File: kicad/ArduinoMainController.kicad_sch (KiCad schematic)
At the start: 3 parts

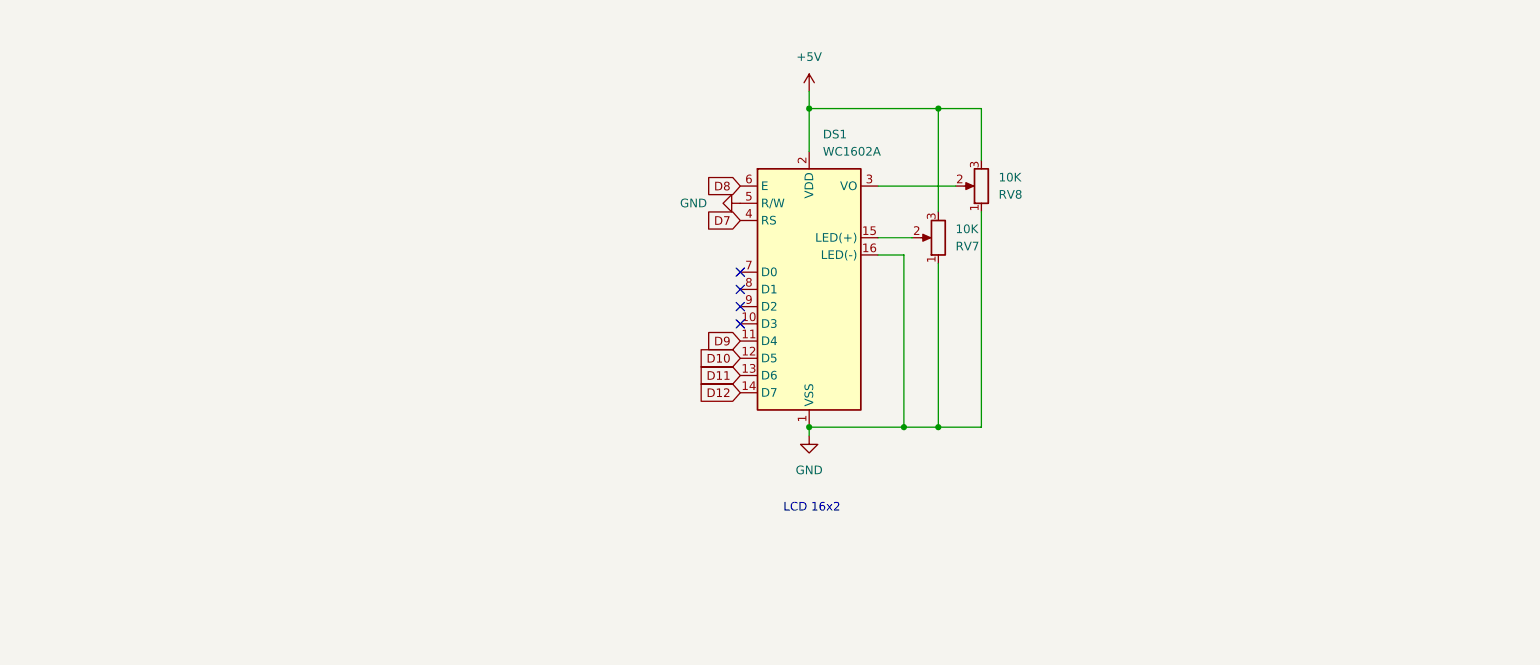
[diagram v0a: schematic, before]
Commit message: Cambio Arduino por el ATMega328
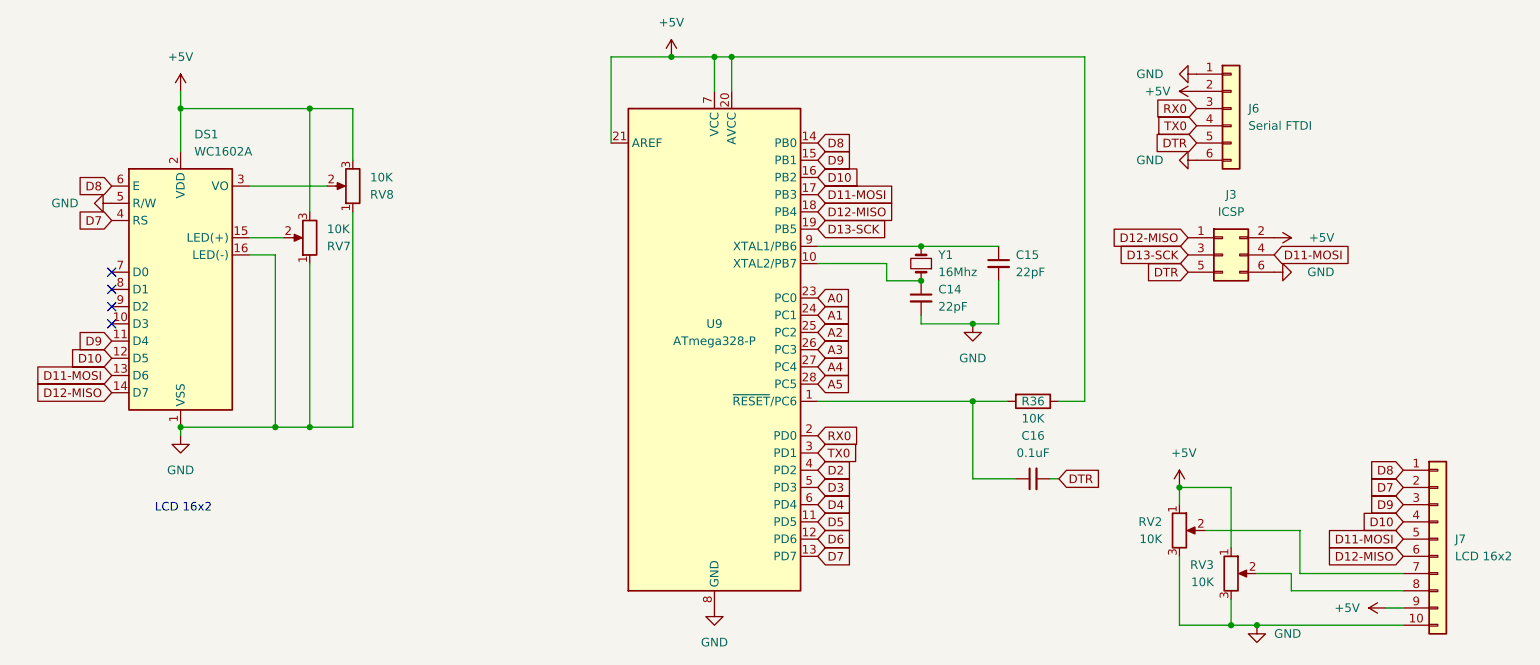
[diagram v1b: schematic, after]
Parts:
- added C14, C15: 22pF, Capacitor_THT:C_Disc_D3.0mm_W1.6mm_P2.50mm, symbol Device:C_Small
- added C16: 0.1uF, Capacitor_THT:C_Disc_D3.0mm_W1.6mm_P2.50mm, symbol Device:C_Small
- added J3: ICSP, Connector_PinSocket_2.54mm:PinSocket_2x03_P2.54mm_Vertical, symbol Connector_Generic:Conn_02x03_Odd_Even
- added J6: Serial FTDI, Connector_PinSocket_2.54mm:PinSocket_1x06_P2.54mm_Vertical, symbol Connector_Generic:Conn_01x06
- added J7: LCD 16x2, Connector_PinSocket_2.54mm:PinSocket_1x10_P2.54mm_Vertical, symbol Connector_Generic:Conn_01x10
- added R36: 10K, Resistor_THT:R_Axial_DIN0207_L6.3mm_D2.5mm_P7.62mm_Horizontal, symbol Device:R
- added RV2, RV3: 10K, Potentiometer_THT:Potentiometer_Bourns_3296W_Vertical, symbol Device:R_Potentiometer
- added U9: ATmega328-P, Package_DIP:DIP-28_W7.62mm, symbol MCU_Microchip_ATmega:ATmega328-P
- added Y1: 16Mhz, Crystal:Crystal_HC18-U_Vertical, symbol Device:Crystal_Small
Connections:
- net +5V: now also J3.2 (Pin_2), J6.2 (Pin_2), J7.9 (Pin_9), R36.1, RV2.1, RV3.1, U9.20 (AVCC), U9.21 (AREF), U9.7 (VCC)
- net D10: now also J7.4 (Pin_4), U9.16 (PB2)
- net D7: now also J7.2 (Pin_2), U9.13 (PD7)
- net D8: now also J7.1 (Pin_1), U9.14 (PB0)
- net D9: now also J7.3 (Pin_3), U9.15 (PB1)
- net GND: now also C14.2, C15.2, J3.6 (Pin_6), J6.1 (Pin_1), J6.6 (Pin_6), J7.10 (Pin_10), RV2.3, RV3.3, U9.22 (GND), U9.8 (GND)
- net D11 renamed D11-MOSI
- net D11-MOSI: now also J3.4 (Pin_4), J7.5 (Pin_5), U9.17 (PB3)
- net D12 renamed D12-MISO
- net D12-MISO: now also J3.1 (Pin_1), J7.6 (Pin_6), U9.18 (PB4)
- new net: J7.7 (Pin_7), RV2.2
- new net: C14.1, U9.10 (XTAL2/PB7), Y1.1
- new net: C15.1, U9.9 (XTAL1/PB6), Y1.2
- new net: C16.1, R36.2, U9.1 (~{RESET}/PC6)
- new net: J7.8 (Pin_8), RV3.2
- new net A0: U9.23 (PC0)
- new net A1: U9.24 (PC1)
- new net A2: U9.25 (PC2)
- new net A3: U9.26 (PC3)
- new net A4: U9.27 (PC4)
- new net A5: U9.28 (PC5)
- new net D13-SCK: J3.3 (Pin_3), U9.19 (PB5)
- new net D2: U9.4 (PD2)
- new net D3: U9.5 (PD3)
- new net D4: U9.6 (PD4)
- new net D5: U9.11 (PD5)
- new net D6: U9.12 (PD6)
- new net DTR: C16.2, J3.5 (Pin_5), J6.5 (Pin_5)
- new net RX0: J6.3 (Pin_3), U9.2 (PD0)
- new net TX0: J6.4 (Pin_4), U9.3 (PD1)
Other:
- moved on the sheet: DS1, RV7, RV8
